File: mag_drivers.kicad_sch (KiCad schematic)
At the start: 29 parts, among them J10 Conn_01x02_Pin, J11 Conn_01x02_Pin, J9 Conn_01x02_Pin, U11 STSPIN250, U2 STSPIN250, U24 AP22652, U8 STSPIN250

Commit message: started layout
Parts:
- C69, C79, C82: footprint (none) -> Capacitor_SMD:C_0201_0603Metric
- J10, J11, J9: footprint (none) -> Connector_JST:JST_SH_BM02B-SRSS-TB_1x02-1MP_P1.00mm_Vertical
- R14, R15, R23, R24, R60, R61, R62, R63, R64: footprint (none) -> Resistor_SMD:R_0402_1005Metric
- R65: footprint Resistor_SMD:R_0603_1608Metric -> Resistor_SMD:R_0402_1005Metric
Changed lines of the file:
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@@
 			)
 		)
-		(property "Footprint" ""
+		(property "Footprint" "Resistor_SMD:R_0402_1005Metric"
 			(at 245.11 135.89 0)
 			(effects
@@
 			)
 		)
-		(property "Footprint" ""
+		(property "Footprint" "Resistor_SMD:R_0402_1005Metric"
 			(at 242.57 64.77 0)
 			(effects
@@
 			)
 		)
-		(property "Footprint" ""
+		(property "Footprint" "Resistor_SMD:R_0402_1005Metric"
 			(at 35.56 46.99 0)
 			(effects
@@
 			)
 		)
-		(property "Footprint" ""
+		(property "Footprint" "Resistor_SMD:R_0402_1005Metric"
 			(at 100.33 63.5 0)
 			(effects
@@
 			)
 		)
-		(property "Footprint" ""
+		(property "Footprint" "Connector_JST:JST_SH_BM02B-SRSS-TB_1x02-1MP_P1.00mm_Vertical"
 			(at 262.89 127 0)
 			(effects
@@
 			)
 		)
-		(property "Footprint" "Resistor_SMD:R_0603_1608Metric"
+		(property "Footprint" "Resistor_SMD:R_0402_1005Metric"
 			(at 55.88 133.35 0)
 			(effects
@@
 			)
 		)
-		(property "Footprint" ""
+		(property "Footprint" "Resistor_SMD:R_0402_1005Metric"
 			(at 180.34 123.19 0)
 			(effects
@@
 			)
 		)
-		(property "Footprint" ""
+		(property "Footprint" "Capacitor_SMD:C_0201_0603Metric"
 			(at 170.18 52.07 0)
 			(effects
@@
 			)
 		)
-		(property "Footprint" ""
+		(property "Footprint" "Capacitor_SMD:C_0201_0603Metric"
 			(at 27.94 50.8 0)
 			(effects
@@
 			)
 		)
-		(property "Footprint" ""
+		(property "Footprint" "Resistor_SMD:R_0402_1005Metric"
 			(at 35.56 50.8 0)
 			(effects
@@
 			)
 		)
-		(property "Footprint" ""
+		(property "Footprint" "Resistor_SMD:R_0402_1005Metric"
 			(at 177.8 52.07 0)
 			(effects
@@
 			)
 		)
-		(property "Footprint" ""
+		(property "Footprint" "Connector_JST:JST_SH_BM02B-SRSS-TB_1x02-1MP_P1.00mm_Vertical"
 			(at 260.35 55.88 0)
 			(effects
@@
 			)
 		)
-		(property "Footprint" ""
+		(property "Footprint" "Resistor_SMD:R_0402_1005Metric"
 			(at 180.34 119.38 0)
 			(effects
@@
 			)
 		)
-		(property "Footprint" ""
+		(property "Footprint" "Connector_JST:JST_SH_BM02B-SRSS-TB_1x02-1MP_P1.00mm_Vertical"
 			(at 118.11 54.61 0)
 			(effects
@@
 			)
 		)
-		(property "Footprint" ""
+		(property "Footprint" "Resistor_SMD:R_0402_1005Metric"
 			(at 177.8 48.26 0)
 			(effects
@@
 			)
 		)
-		(property "Footprint" ""
+		(property "Footprint" "Capacitor_SMD:C_0201_0603Metric"
 			(at 172.72 123.19 0)
 			(effects

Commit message: finished layout of v0.2!
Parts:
- removed U24: AP22652, SOT26:SOT26, symbol Power_Management:AP22652
- added H3, H4, H5, H6, H7, H8, H9: MountingHole, MountingHole:MountingHole_2.5mm_Pad, symbol Mechanical:MountingHole
- added R67: 1k, Resistor_SMD:R_0402_1005Metric, symbol Device:R_Small_US
- added U15: SiP32431DR3, Package_TO_SOT_SMD:SOT-363_SC-70-6, symbol Power_Management:SiP32431DR3
- C85: value 100nf -> 1uF
- C86: value 100nf -> 0.1uF
- R65: value 47k -> 10k; DPN RMCF0603FT47K0CT-ND -> (none); DST Digi-Key -> (none); MFR Stackpole Electronics Inc -> (none); MPN RMCF0603FT47K0 -> (none)
- U11, U2, U8: footprint STSPIN250:QFN50P300X300X100-17N -> footprints:QFN50P300X300X100-17N
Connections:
- net +3V3 is gone; now on net REF1_A_3: R65.1
- net REF1_B_3 is gone; now on net REF1_A_3: U8.11 (REF)
- net REF2_A_3 is gone; now on net REF1_A_3: U11.11 (REF)
- net EN_MAG: now also U15.3 (ON)
- net GND: now also R67.1, U15.2 (GND), U15.5 (GND)
- net MAG_V: now also C86.1, U15.1 (OUT)
- net REF1_A_3: now also R67.2
- net V_POT: now also U15.4 (IN)
- net +3.3V: now reaches R65.2
- no-connect marks 7 -> 6
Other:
- note added: "330mOhm*1A = 0.33V"
- moved on the sheet: C85

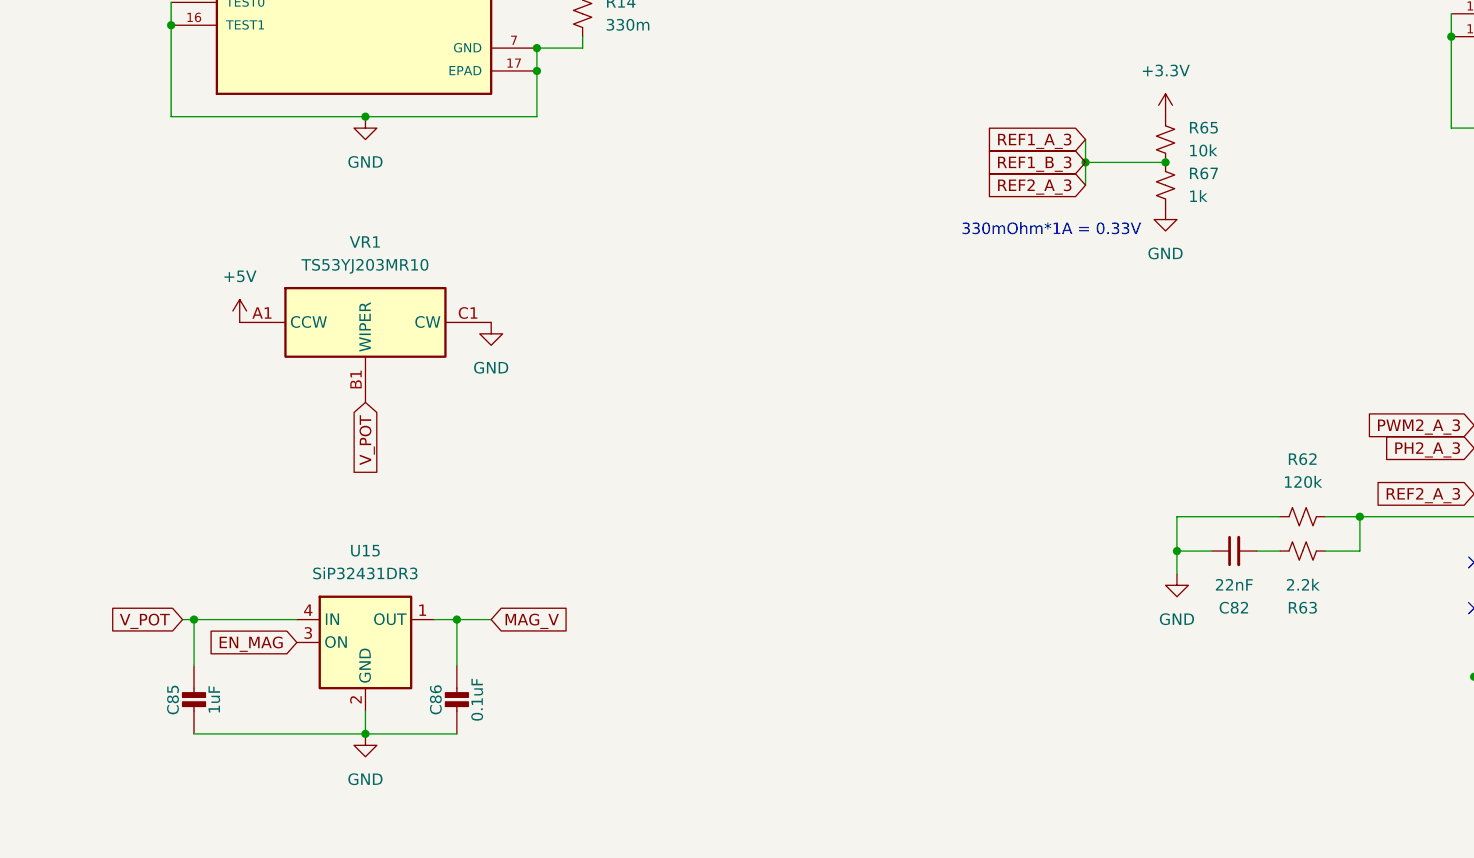
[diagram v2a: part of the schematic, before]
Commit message: added testpoints
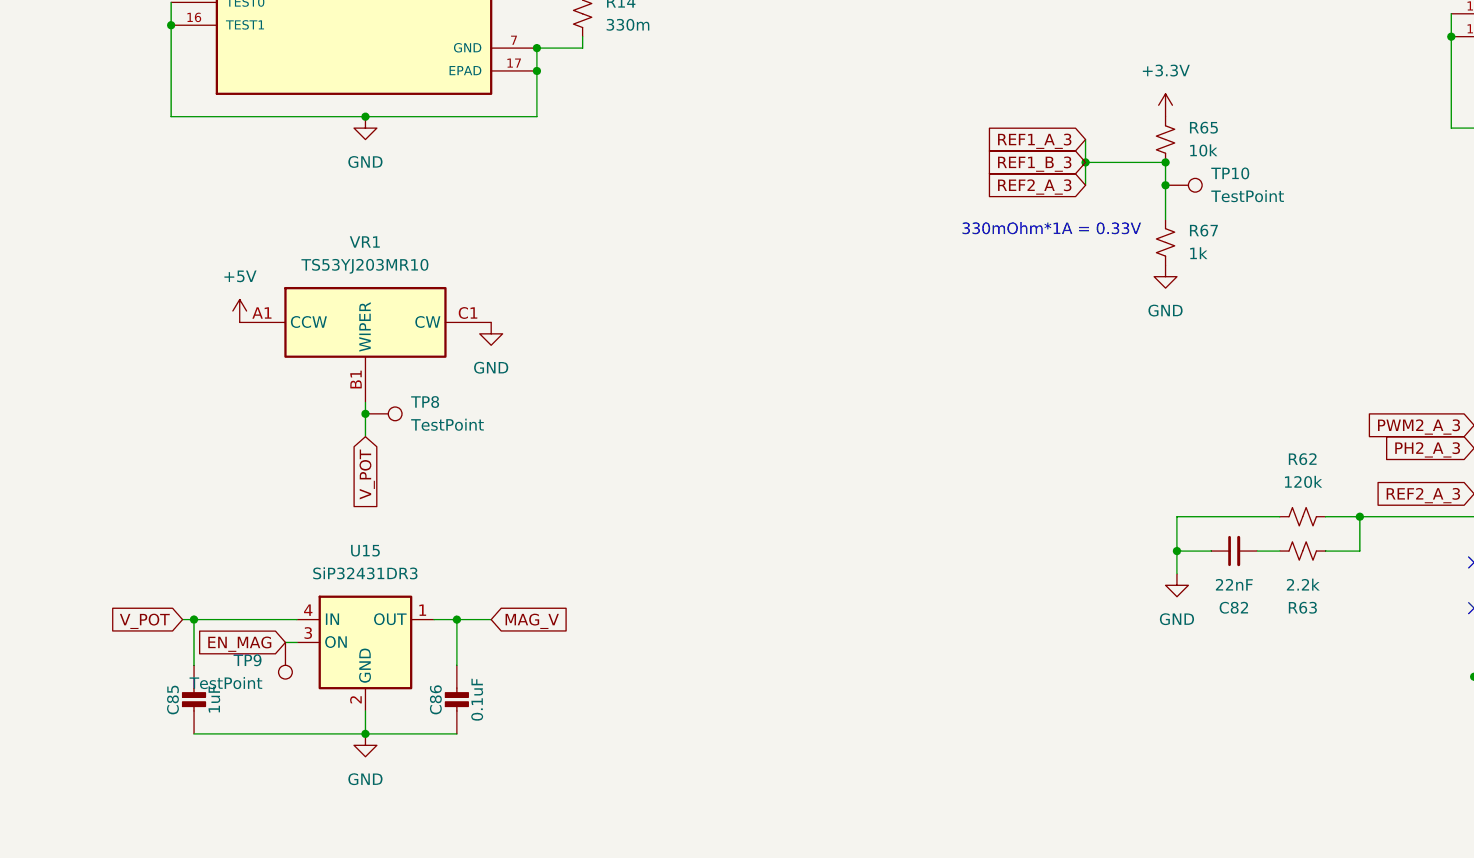
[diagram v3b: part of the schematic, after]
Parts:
- added TP10, TP8, TP9: TestPoint, TestPoint:TestPoint_Pad_D1.5mm, symbol Connector:TestPoint
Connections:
- net EN_MAG: now also TP9.1
- net REF1_A_3: now also TP10.1
- net V_POT: now also TP8.1
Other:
- moved on the sheet: R67
